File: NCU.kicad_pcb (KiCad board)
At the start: 2 copper layers, 22 parts, among them J2 USB_C_Receptacle_USB2.0_14P, J3 Micro_SD_Card, U1 STM32H745ZITx, U2 USB3300-EZK, U3 SN65HVD230, U4 SN65HVD230, U5 XL1509-3.3, U6 ESP32-C3-WROOM-02, U7 AP2112K-1.8, U8 LAN8742A

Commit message: work in progress
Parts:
- added C10: 100nF, Capacitor_SMD:C_0402_1005Metric_Pad0.74x0.62mm_HandSolder, F.Cu at (165.2, 59.0)
- added C11: 100nF, Capacitor_SMD:C_0402_1005Metric_Pad0.74x0.62mm_HandSolder, F.Cu at (165.2, 61.0)
- added C12: 100nF, Capacitor_SMD:C_0402_1005Metric_Pad0.74x0.62mm_HandSolder, F.Cu at (165.2, 62.9)
- added C13: 100nF, Capacitor_SMD:C_0402_1005Metric_Pad0.74x0.62mm_HandSolder, F.Cu at (165.2, 64.9)
- added C14: 100nF, Capacitor_SMD:C_0402_1005Metric_Pad0.74x0.62mm_HandSolder, F.Cu at (165.2, 66.9)
- added C15: 100nF, Capacitor_SMD:C_0402_1005Metric_Pad0.74x0.62mm_HandSolder, F.Cu at (165.2, 68.8)
- added C16: 100nF, Capacitor_SMD:C_0402_1005Metric_Pad0.74x0.62mm_HandSolder, F.Cu at (168.5, 57.0)
- added C17: 100nF, Capacitor_SMD:C_0402_1005Metric_Pad0.74x0.62mm_HandSolder, F.Cu at (168.5, 59.0)
- added C18: 100nF, Capacitor_SMD:C_0402_1005Metric_Pad0.74x0.62mm_HandSolder, F.Cu at (168.5, 61.0)
- added C19: 100nF, Capacitor_SMD:C_0402_1005Metric_Pad0.74x0.62mm_HandSolder, F.Cu at (168.5, 62.9)
- added C20: 100nF, Capacitor_SMD:C_0402_1005Metric_Pad0.74x0.62mm_HandSolder, F.Cu at (168.5, 64.9)
- added C21: 100nF, Capacitor_SMD:C_0402_1005Metric_Pad0.74x0.62mm_HandSolder, F.Cu at (168.5, 66.9)
- added C22: 100nF, Capacitor_SMD:C_0402_1005Metric_Pad0.74x0.62mm_HandSolder, F.Cu at (168.5, 68.8)
- added C23: 100nF, Capacitor_SMD:C_0402_1005Metric_Pad0.74x0.62mm_HandSolder, F.Cu at (171.7, 57.0)
- added C24: 100nF, Capacitor_SMD:C_0402_1005Metric_Pad0.74x0.62mm_HandSolder, F.Cu at (171.7, 59.0)
- added C25: 100nF, Capacitor_SMD:C_0402_1005Metric_Pad0.74x0.62mm_HandSolder, F.Cu at (171.7, 61.0)
- added C26: 100nF, Capacitor_SMD:C_0402_1005Metric_Pad0.74x0.62mm_HandSolder, F.Cu at (171.7, 62.9)
- added C27: 4.7uF, Capacitor_SMD:C_0402_1005Metric_Pad0.74x0.62mm_HandSolder, F.Cu at (171.7, 64.9)
- added C28: 200nF, Capacitor_SMD:C_0402_1005Metric_Pad0.74x0.62mm_HandSolder, F.Cu at (176.9, 57.0)
- added C29: 200nF, Capacitor_SMD:C_0402_1005Metric_Pad0.74x0.62mm_HandSolder, F.Cu at (176.9, 59.0)
- added C9: 4.7uF, Capacitor_SMD:C_0402_1005Metric_Pad0.74x0.62mm_HandSolder, F.Cu at (165.2, 57.0)
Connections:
- U1 pad 103: unconnected-(U1-VCAP-Pad103) -> Net-(C28-Pad1)
- U1 pad 104: Net-(U1-VSS-Pad104) -> GND
- U1 pad 105: unconnected-(U1-VDDLDO-Pad105) -> /MCU/3V3
- U1 pad 106: unconnected-(U1-VDD-Pad106) -> /MCU/3V3
- U1 pad 118: Net-(U1-VSS-Pad104) -> GND
- U1 pad 119: unconnected-(U1-VDD-Pad119) -> /MCU/3V3
- U1 pad 12: Net-(U1-VSS-Pad104) -> GND
- U1 pad 128: Net-(U1-VSS-Pad104) -> GND
- U1 pad 129: unconnected-(U1-VDD-Pad129) -> /MCU/3V3
- U1 pad 13: unconnected-(U1-VDD-Pad13) -> /MCU/3V3
- U1 pad 14: unconnected-(U1-VSSSMPS-Pad14) -> GND
- U1 pad 140: unconnected-(U1-VCAP-Pad140) -> Net-(C28-Pad1)
- U1 pad 141: Net-(U1-VSS-Pad104) -> GND
- U1 pad 143: unconnected-(U1-VDDLDO-Pad143) -> /MCU/3V3
- U1 pad 144: unconnected-(U1-VDD-Pad144) -> /MCU/3V3
- U1 pad 16: unconnected-(U1-VDDSMPS-Pad16) -> /MCU/MCU Power/VSSSMPS
- U1 pad 18: Net-(U1-VSS-Pad104) -> GND
- U1 pad 19: unconnected-(U1-VDD-Pad19) -> /MCU/3V3
- U1 pad 32: unconnected-(U1-VDD-Pad32) -> /MCU/3V3
- U1 pad 33: Net-(U1-VSS-Pad104) -> GND
- U1 pad 34: unconnected-(U1-VSSA-Pad34) -> GND
- U1 pad 36: unconnected-(U1-VDDA-Pad36) -> /MCU/3V3
- U1 pad 41: Net-(U1-VSS-Pad104) -> GND
- U1 pad 42: unconnected-(U1-VDD-Pad42) -> /MCU/3V3
- U1 pad 55: Net-(U1-VSS-Pad104) -> GND
- U1 pad 56: unconnected-(U1-VDD-Pad56) -> /MCU/3V3
- U1 pad 6: Net-(U1-VSS-Pad104) -> GND
- U1 pad 68: unconnected-(U1-VCAP-Pad68) -> Net-(C28-Pad1)
- U1 pad 69: Net-(U1-VSS-Pad104) -> GND
- U1 pad 7: unconnected-(U1-VDD-Pad7) -> /MCU/3V3
- U1 pad 70: unconnected-(U1-VDDLDO-Pad70) -> /MCU/3V3
- U1 pad 71: unconnected-(U1-VDD-Pad71) -> /MCU/3V3
- U1 pad 79: unconnected-(U1-VDD-Pad79) -> /MCU/3V3
- U1 pad 8: unconnected-(U1-VBAT-Pad8) -> /MCU/3V3
- U1 pad 80: Net-(U1-VSS-Pad104) -> GND
- U1 pad 89: Net-(U1-VSS-Pad104) -> GND
- U1 pad 90: unconnected-(U1-VDD50_USB-Pad90) -> /MCU/3V3
- U1 pad 91: unconnected-(U1-VDD33_USB-Pad91) -> /MCU/3V3
- U1 pad 92: unconnected-(U1-VDD-Pad92) -> /MCU/3V3

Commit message: wip
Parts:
- added C30: 100nF, Capacitor_SMD:C_0402_1005Metric_Pad0.74x0.62mm_HandSolder, F.Cu at (96.2, 65.1)
- added J1: RJ45, Connector_RJ:RJ45_Hanrun_HR911105A_Horizontal, F.Cu at (75.3, 43.8)
- added J3: Micro_SD_Card, Connector_Card:microSD_HC_Molex_47219-2001, F.Cu at (98.1, 46.8)
- added U9: BG95-M3, RF_GSM:Quectel_BG95, F.Cu at (81.2, 77.4)
- C23, C25: value 100nF -> 1uF
- C28, C29: value 200nF -> 2.2uF
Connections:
- net Net-(J2-CC1) renamed /USB/CC1
- net Net-(J2-CC2) renamed /USB/CC2
- net Net-(J2-D+-PadA6) renamed /USB/D+
- net Net-(J2-D--PadA7) renamed /USB/D-
- C27 pad 2: /MCU/MCU Power/VSSSMPS -> GND
- U1 pad 16: /MCU/MCU Power/VSSSMPS -> /MCU/3V3

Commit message: updated to use RMII and routed ethernet and CAN from micro
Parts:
- added C31: 220pF, Capacitor_SMD:C_0402_1005Metric_Pad0.74x0.62mm_HandSolder, F.Cu at (117.1, 49.0)
- added C32: 10uF, Capacitor_SMD:C_0402_1005Metric_Pad0.74x0.62mm_HandSolder, F.Cu at (117.1, 51.0)
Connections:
- C10 pad 1: /MCU/3V3 -> +3V3
- C11 pad 1: /MCU/3V3 -> +3V3
- C12 pad 1: /MCU/3V3 -> +3V3
- C13 pad 1: /MCU/3V3 -> +3V3
- C14 pad 1: /MCU/3V3 -> +3V3
- C15 pad 1: /MCU/3V3 -> +3V3
- C16 pad 1: /MCU/3V3 -> +3V3
- C17 pad 1: /MCU/3V3 -> +3V3
- C18 pad 1: /MCU/3V3 -> +3V3
- C19 pad 1: /MCU/3V3 -> +3V3
- C20 pad 1: /MCU/3V3 -> +3V3
- C21 pad 1: /MCU/3V3 -> +3V3
- C22 pad 1: /MCU/3V3 -> +3V3
- C23 pad 1: /MCU/3V3 -> +3V3
- C24 pad 1: /MCU/3V3 -> +3V3
- C25 pad 1: /MCU/3V3 -> +3V3
- C26 pad 1: /MCU/3V3 -> +3V3
- C27 pad 1: /MCU/3V3 -> +3V3
- C30 pad 1: /MCU/3V3 -> +3V3
- C9 pad 1: /MCU/3V3 -> +3V3
- U1 pad 105: /MCU/3V3 -> +3V3
- U1 pad 106: /MCU/3V3 -> +3V3
- U1 pad 112: unconnected-(U1-PD0-Pad112) -> /MCU/FDCAN1_RX
- U1 pad 113: unconnected-(U1-PD1-Pad113) -> /MCU/FDCAN1_TX
- U1 pad 119: /MCU/3V3 -> +3V3
- U1 pad 129: /MCU/3V3 -> +3V3
- U1 pad 13: /MCU/3V3 -> +3V3
- U1 pad 132: unconnected-(U1-PB5-Pad132) -> /MCU/FDCAN2_RX
- U1 pad 133: unconnected-(U1-PB6-Pad133) -> /MCU/FDCAN2_TX
- U1 pad 143: /MCU/3V3 -> +3V3
- U1 pad 144: /MCU/3V3 -> +3V3
- U1 pad 15: unconnected-(U1-VLXSMPS-Pad15) -> Net-(U1-VLXSMPS)
- U1 pad 16: /MCU/3V3 -> +3V3
- U1 pad 17: unconnected-(U1-VFBSMPS-Pad17) -> Net-(U1-VFBSMPS)
- U1 pad 19: /MCU/3V3 -> +3V3
- U1 pad 29: unconnected-(U1-PC1-Pad29) -> /MCU/ETH_MDC
- U1 pad 32: /MCU/3V3 -> +3V3
- U1 pad 35: unconnected-(U1-VREF+-Pad35) -> +3V3
- U1 pad 36: /MCU/3V3 -> +3V3
- U1 pad 39: unconnected-(U1-PA2-Pad39) -> /MCU/ETH_MDIO
- U1 pad 42: /MCU/3V3 -> +3V3
- U1 pad 46: unconnected-(U1-PA7-Pad46) -> /MCU/ETH_CRS_DV
- U1 pad 47: unconnected-(U1-PC4-Pad47) -> /MCU/ETH_RXD0
- U1 pad 48: unconnected-(U1-PC5-Pad48) -> /MCU/ETH_RXD1
- U1 pad 56: /MCU/3V3 -> +3V3
- U1 pad 67: unconnected-(U1-PB11-Pad67) -> /MCU/ETH_TX_EN
- U1 pad 7: /MCU/3V3 -> +3V3
- U1 pad 70: /MCU/3V3 -> +3V3
- U1 pad 71: /MCU/3V3 -> +3V3
- U1 pad 72: unconnected-(U1-PB12-Pad72) -> /MCU/ETH_TXD0
- U1 pad 73: unconnected-(U1-PB13-Pad73) -> /MCU/ETH_TXD1
- U1 pad 79: /MCU/3V3 -> +3V3
- U1 pad 8: /MCU/3V3 -> +3V3
- U1 pad 90: /MCU/3V3 -> +3V3
- U1 pad 91: /MCU/3V3 -> +3V3
- U1 pad 92: /MCU/3V3 -> +3V3
- U8 pad 10: unconnected-(U8-RXER/PHYAD0-Pad10) -> GND
- U8 pad 11: unconnected-(U8-CRS_DV/MODE2-Pad11) -> /MCU/ETH_CRS_DV
- U8 pad 12: unconnected-(U8-MDIO-Pad12) -> /MCU/ETH_MDIO
- U8 pad 13: unconnected-(U8-MDC-Pad13) -> /MCU/ETH_MDC
- U8 pad 16: unconnected-(U8-TXEN-Pad16) -> /MCU/ETH_TX_EN
- U8 pad 17: unconnected-(U8-TXD0-Pad17) -> /MCU/ETH_TXD0
- U8 pad 18: unconnected-(U8-TXD1-Pad18) -> /MCU/ETH_TXD1
- U8 pad 7: unconnected-(U8-RXD1/MODE1-Pad7) -> /MCU/ETH_RXD1
- U8 pad 8: unconnected-(U8-RXD0/MODE0-Pad8) -> /MCU/ETH_RXD0

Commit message: full initial power scheme
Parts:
- added C33: 4.7uF, Capacitor_SMD:C_1210_3225Metric_Pad1.33x2.70mm_HandSolder, F.Cu at (110.1, 113.8)
- added C34: 4.7uF, Capacitor_SMD:C_1210_3225Metric_Pad1.33x2.70mm_HandSolder, F.Cu at (110.1, 118.0)
- added C35: 0.1uF, Capacitor_SMD:C_0603_1608Metric_Pad1.08x0.95mm_HandSolder, F.Cu at (118.5, 122.4)
- added C36: 0.1uF, Capacitor_SMD:C_0402_1005Metric_Pad0.74x0.62mm_HandSolder, F.Cu at (118.0, 124.7)
- added C37: 33pF, Capacitor_SMD:C_0402_1005Metric_Pad0.74x0.62mm_HandSolder, F.Cu at (118.0, 126.6)
- added C38: 47uF, Capacitor_SMD:C_1210_3225Metric_Pad1.33x2.70mm_HandSolder, F.Cu at (110.1, 122.2)
- added C39: 47uF, Capacitor_SMD:C_1210_3225Metric_Pad1.33x2.70mm_HandSolder, F.Cu at (110.1, 126.5)
- added IC1: LMR51460SQDRRRQ1, SamacSys_Parts:SON50P300X300X80-13N-D, F.Cu at (126.5, 127.5)
- added IC2: TPS628101HQWRWYRQ1, SamacSys_Parts:TPS6281008QWRWYRQ1, F.Cu at (99.0, 120.1)
- added L1: 0.47uH, SamacSys_Parts:INDPM7066X240N, F.Cu at (134.5, 119.5)
- added L3: 4.7uH, Inductor_SMD:L_Coilcraft_XAL7030-472, F.Cu at (121.1, 116.4)
- added Q1: CSD25483F4, SamacSys_Parts:CSD25483F4T, F.Cu at (136.2, 129.3)
- added Q2: CSD25483F4, SamacSys_Parts:CSD25483F4T, F.Cu at (136.2, 133.0)
- added R1: 100k, Resistor_SMD:R_0402_1005Metric_Pad0.72x0.64mm_HandSolder, F.Cu at (114.7, 112.6)
- added R2: 19.1k, Resistor_SMD:R_0402_1005Metric_Pad0.72x0.64mm_HandSolder, F.Cu at (114.7, 114.6)
- added R3: 1k, Resistor_SMD:R_0402_1005Metric_Pad0.72x0.64mm_HandSolder, F.Cu at (114.7, 116.6)
- added R4: 100k, Resistor_SMD:R_0402_1005Metric_Pad0.72x0.64mm_HandSolder, F.Cu at (114.7, 118.6)
- added R5: 10k, Resistor_SMD:R_0402_1005Metric_Pad0.72x0.64mm_HandSolder, F.Cu at (114.7, 120.6)
- added R6: 100k, Resistor_SMD:R_0402_1005Metric_Pad0.72x0.64mm_HandSolder, F.Cu at (114.7, 122.6)
- added R7: 10k, Resistor_SMD:R_0402_1005Metric_Pad0.72x0.64mm_HandSolder, F.Cu at (114.7, 124.6)
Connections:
- U1 pad 100: unconnected-(U1-PA11-Pad100) -> /MCU/USB_OTG_FS_DM
- U1 pad 101: unconnected-(U1-PA12-Pad101) -> /MCU/USB_OTG_FS_DP
- U1 pad 98: unconnected-(U1-PA9-Pad98) -> /MCU/USB_OTG_FS_VBUS
- U3 pad 1: /CAN/CAN0_TX -> /MCU/FDCAN1_TX
- U3 pad 4: /CAN/CAN0_RX -> /MCU/FDCAN1_RX
- U4 pad 1: /CAN/CAN1_TX -> /MCU/FDCAN2_TX
- U4 pad 4: /CAN/CAN1_RX -> /MCU/FDCAN2_RX

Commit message: added lib to project and added molex superseal connector
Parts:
- added C40: 4.7nF, Capacitor_SMD:C_0402_1005Metric_Pad0.74x0.62mm_HandSolder, F.Cu at (88.7, 132.2)
- added C41: 10pF, Capacitor_SMD:C_0402_1005Metric_Pad0.74x0.62mm_HandSolder, F.Cu at (88.7, 134.2)
- added C42: 100nF, Capacitor_SMD:C_0402_1005Metric_Pad0.74x0.62mm_HandSolder, F.Cu at (85.7, 97.6)
- added C43: 100nF, Capacitor_SMD:C_0402_1005Metric_Pad0.74x0.62mm_HandSolder, F.Cu at (85.7, 99.6)
- added C44: 100nF, Capacitor_SMD:C_0402_1005Metric_Pad0.74x0.62mm_HandSolder, F.Cu at (85.7, 101.5)
- added C45: 100nF, Capacitor_SMD:C_0402_1005Metric_Pad0.74x0.62mm_HandSolder, F.Cu at (85.7, 103.5)
- added C46: 100nF, Capacitor_SMD:C_0402_1005Metric_Pad0.74x0.62mm_HandSolder, F.Cu at (85.7, 105.5)
- added C47: 100nF, Capacitor_SMD:C_0402_1005Metric_Pad0.74x0.62mm_HandSolder, F.Cu at (85.7, 107.5)
- added C48: 100nF, Capacitor_SMD:C_0402_1005Metric_Pad0.74x0.62mm_HandSolder, F.Cu at (85.7, 109.4)
- added C49: 100nF, Capacitor_SMD:C_0402_1005Metric_Pad0.74x0.62mm_HandSolder, F.Cu at (85.7, 111.4)
- added C5: 22uF, Inductor_SMD:L_1206_3216Metric_Pad1.22x1.90mm_HandSolder, F.Cu at (80.8, 130.4)
- added C50: 100nF, Capacitor_SMD:C_0402_1005Metric_Pad0.74x0.62mm_HandSolder, F.Cu at (85.7, 113.4)
- added C6: 22uF, Inductor_SMD:L_1206_3216Metric_Pad1.22x1.90mm_HandSolder, F.Cu at (80.8, 133.9)
- added C7: 22uF, Inductor_SMD:L_1206_3216Metric_Pad1.22x1.90mm_HandSolder, F.Cu at (80.8, 137.3)
- added C8: 22uF, Capacitor_SMD:C_0603_1608Metric_Pad1.08x0.95mm_HandSolder, F.Cu at (86.0, 129.9)
- added D1: BZV55C3V6, Diode_SMD:D_MiniMELF, F.Cu at (81.0, 98.3)
- added D2: BZV55C3V6, Diode_SMD:D_MiniMELF, F.Cu at (81.0, 101.6)
- added D3: BZV55C3V6, Diode_SMD:D_MiniMELF, F.Cu at (81.0, 105.0)
- added D4: BZV55C3V6, Diode_SMD:D_MiniMELF, F.Cu at (81.0, 108.3)
- added D5: BZV55C3V6, Diode_SMD:D_MiniMELF, F.Cu at (81.0, 111.7)
- added D6: BZV55C3V6, Diode_SMD:D_MiniMELF, F.Cu at (81.0, 115.0)
- added D7: BZV55C3V6, Diode_SMD:D_MiniMELF, F.Cu at (81.0, 118.3)
- added D8: BZV55C3V6, Diode_SMD:D_MiniMELF, F.Cu at (81.0, 121.7)
- added D9: BZV55C3V6, Diode_SMD:D_MiniMELF, F.Cu at (81.0, 125.0)
- added J2: USB_B, Connector_USB:USB_B_Lumberg_2411_02_Horizontal, F.Cu at (31.6, 142.2)
- added J4: 6437288-1, SamacSys_Parts:6437288-1, F.Cu at (52.4, 97.4)
- added NT1: NetTie_2, NetTie:NetTie-2_SMD_Pad0.5mm, F.Cu at (88.4, 135.9)
- added R10: 19.6k, Resistor_SMD:R_0402_1005Metric_Pad0.72x0.64mm_HandSolder, F.Cu at (85.5, 136.2)
- added R11: 100k, Resistor_SMD:R_0402_1005Metric_Pad0.72x0.64mm_HandSolder, F.Cu at (85.5, 138.2)
- added R12: 100k, Resistor_SMD:R_0402_1005Metric_Pad0.72x0.64mm_HandSolder, F.Cu at (85.5, 140.2)
- added R13: 100, Capacitor_SMD:C_0402_1005Metric_Pad0.74x0.62mm_HandSolder, F.Cu at (89.0, 97.6)
- added R14: 10k, Capacitor_SMD:C_0402_1005Metric_Pad0.74x0.62mm_HandSolder, F.Cu at (89.0, 99.6)
- added R15: 20k, Capacitor_SMD:C_0402_1005Metric_Pad0.74x0.62mm_HandSolder, F.Cu at (89.0, 101.5)
- added R16: 10k, Capacitor_SMD:C_0402_1005Metric_Pad0.74x0.62mm_HandSolder, F.Cu at (89.0, 103.5)
- added R17: 20k, Capacitor_SMD:C_0402_1005Metric_Pad0.74x0.62mm_HandSolder, F.Cu at (89.0, 105.5)
- added R18: 100, Capacitor_SMD:C_0402_1005Metric_Pad0.74x0.62mm_HandSolder, F.Cu at (89.0, 107.5)
- added R19: 10k, Capacitor_SMD:C_0402_1005Metric_Pad0.74x0.62mm_HandSolder, F.Cu at (89.0, 109.4)
- added R20: 20k, Capacitor_SMD:C_0402_1005Metric_Pad0.74x0.62mm_HandSolder, F.Cu at (89.0, 111.4)
- added R21: 100, Capacitor_SMD:C_0402_1005Metric_Pad0.74x0.62mm_HandSolder, F.Cu at (89.0, 113.4)
- added R22: 10k, Capacitor_SMD:C_0402_1005Metric_Pad0.74x0.62mm_HandSolder, F.Cu at (92.2, 97.6)
- added R23: 20k, Capacitor_SMD:C_0402_1005Metric_Pad0.74x0.62mm_HandSolder, F.Cu at (92.2, 99.6)
- added R24: 100, Capacitor_SMD:C_0402_1005Metric_Pad0.74x0.62mm_HandSolder, F.Cu at (92.2, 101.5)
- added R25: 10k, Capacitor_SMD:C_0402_1005Metric_Pad0.74x0.62mm_HandSolder, F.Cu at (92.2, 103.5)
- added R26: 20k, Capacitor_SMD:C_0402_1005Metric_Pad0.74x0.62mm_HandSolder, F.Cu at (92.2, 105.5)
- added R27: 100, Capacitor_SMD:C_0402_1005Metric_Pad0.74x0.62mm_HandSolder, F.Cu at (92.2, 107.5)
- added R28: 10k, Capacitor_SMD:C_0402_1005Metric_Pad0.74x0.62mm_HandSolder, F.Cu at (92.2, 109.4)
- added R29: 20k, Capacitor_SMD:C_0402_1005Metric_Pad0.74x0.62mm_HandSolder, F.Cu at (92.2, 111.4)
- added R30: 100, Capacitor_SMD:C_0402_1005Metric_Pad0.74x0.62mm_HandSolder, F.Cu at (92.2, 113.4)
- added R31: 10k, Capacitor_SMD:C_0402_1005Metric_Pad0.74x0.62mm_HandSolder, F.Cu at (95.4, 97.6)
- added R32: 20k, Capacitor_SMD:C_0402_1005Metric_Pad0.74x0.62mm_HandSolder, F.Cu at (95.4, 99.6)
- added R33: 100, Capacitor_SMD:C_0402_1005Metric_Pad0.74x0.62mm_HandSolder, F.Cu at (95.4, 101.5)
- added R34: 10k, Capacitor_SMD:C_0402_1005Metric_Pad0.74x0.62mm_HandSolder, F.Cu at (95.4, 103.5)
- added R35: 20k, Capacitor_SMD:C_0402_1005Metric_Pad0.74x0.62mm_HandSolder, F.Cu at (95.4, 105.5)
- added R36: 100, Capacitor_SMD:C_0402_1005Metric_Pad0.74x0.62mm_HandSolder, F.Cu at (95.4, 107.5)
- added R37: 10k, Capacitor_SMD:C_0402_1005Metric_Pad0.74x0.62mm_HandSolder, F.Cu at (95.4, 109.4)
- added R38: 20k, Capacitor_SMD:C_0402_1005Metric_Pad0.74x0.62mm_HandSolder, F.Cu at (95.4, 111.4)
- added R39: 100, Capacitor_SMD:C_0402_1005Metric_Pad0.74x0.62mm_HandSolder, F.Cu at (95.4, 113.4)
- added R8: 8.06k, Resistor_SMD:R_0402_1005Metric_Pad0.72x0.64mm_HandSolder, F.Cu at (85.5, 132.2)
- added R9: 88.7k, Resistor_SMD:R_0402_1005Metric_Pad0.72x0.64mm_HandSolder, F.Cu at (85.5, 134.2)
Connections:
- net /Power Supplies/SW_FB renamed /Power Supplies/LMR_FB
- IC1 pad 5: unconnected-(IC1-PG-Pad5) -> /Power Supplies/12V_PG
- IC2 pad 1: unconnected-(IC2-MODE/SYNC_1-Pad1) -> +5V
- IC2 pad 10: unconnected-(IC2-MODE/SYNC_2-Pad10) -> +5V
- IC2 pad 11: unconnected-(IC2-FB_2-Pad11) -> /Power Supplies/TPS_FB
- IC2 pad 12: unconnected-(IC2-COMP/_FSET_2-Pad12) -> /Power Supplies/TPS_CF
- IC2 pad 13: unconnected-(IC2-EN_2-Pad13) -> +5V
- IC2 pad 2: unconnected-(IC2-VIN-Pad2) -> +5V
- IC2 pad 3: unconnected-(IC2-SW-Pad3) -> Net-(IC2-SW)
- IC2 pad 4: unconnected-(IC2-GND-Pad4) -> GND
- IC2 pad 5: unconnected-(IC2-FB_1-Pad5) -> /Power Supplies/TPS_FB
- IC2 pad 6: unconnected-(IC2-SS/TR-Pad6) -> Net-(IC2-SS/TR)
- IC2 pad 7: unconnected-(IC2-COMP/_FSET_1-Pad7) -> /Power Supplies/TPS_CF
- IC2 pad 8: unconnected-(IC2-EN_1-Pad8) -> +5V
- IC2 pad 9: unconnected-(IC2-PG-Pad9) -> /Power Supplies/3V3_PG
- L1 pad 1: unconnected-(L1-Pad1) -> Net-(IC2-SW)
- L1 pad 2: unconnected-(L1-Pad2) -> +3V3

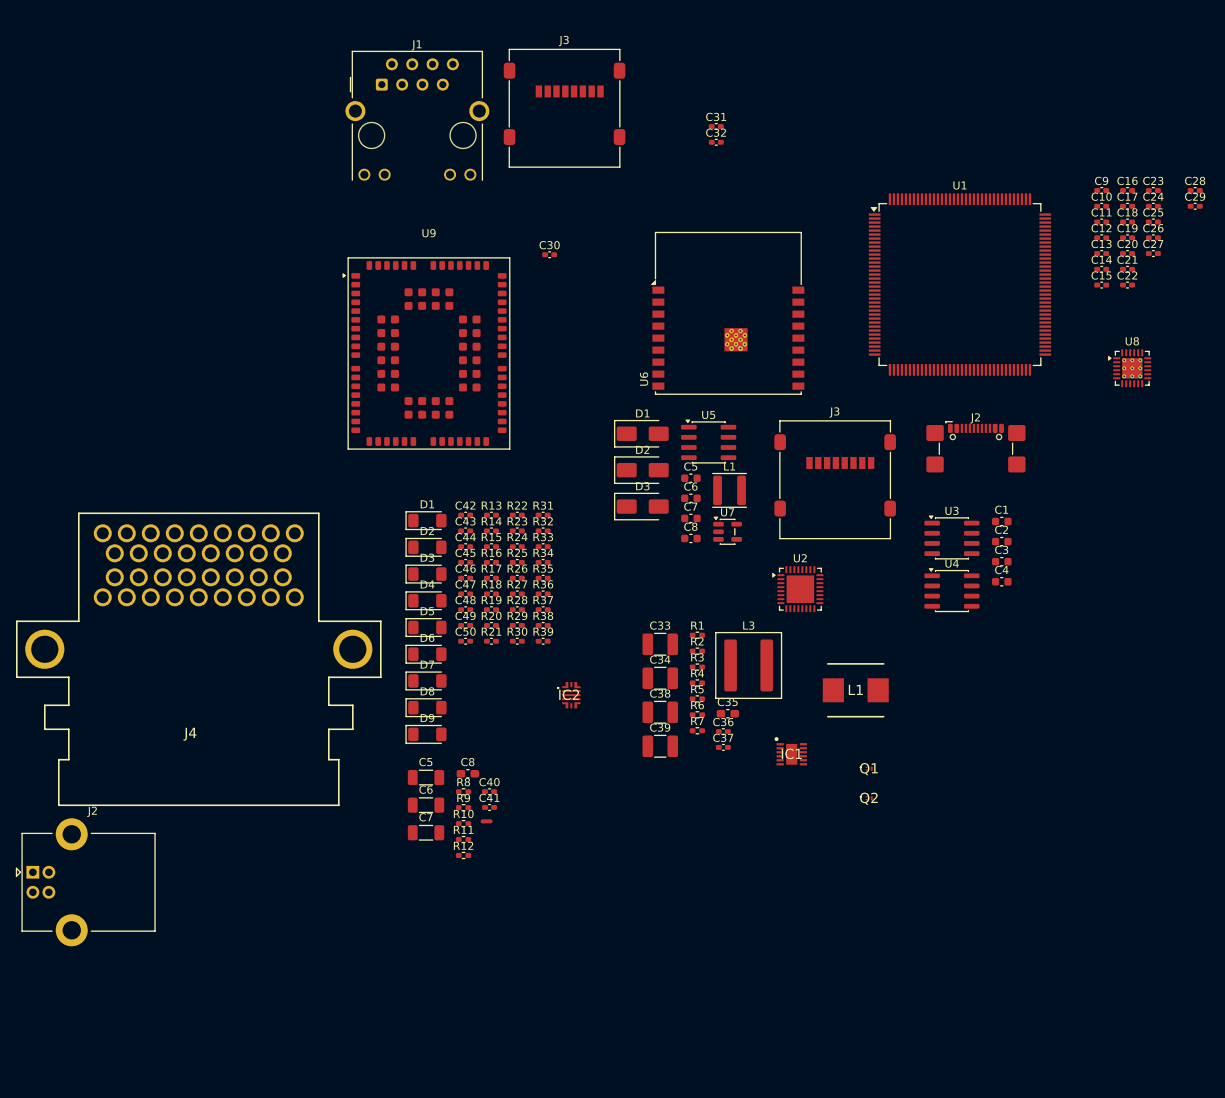
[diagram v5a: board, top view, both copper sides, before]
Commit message: added connects schematic, which is looking quite good
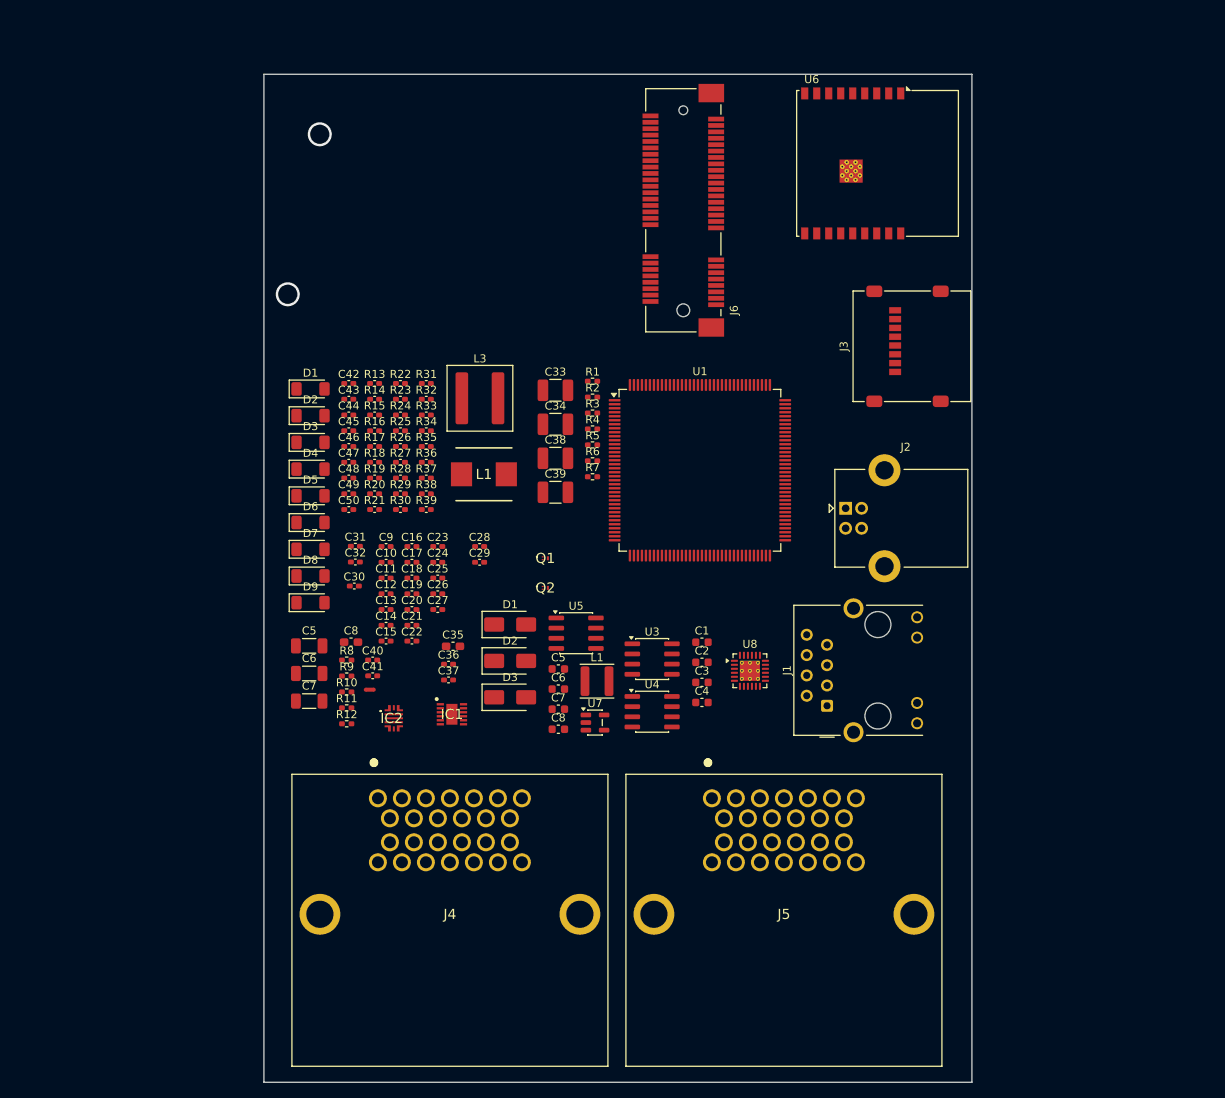
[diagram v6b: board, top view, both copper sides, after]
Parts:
- removed the J2 at (149.5, 90.4)
- removed the J3 at (98.1, 46.8)
- removed U2: USB3300-EZK, Package_DFN_QFN:QFN-32-1EP_5x5mm_P0.5mm_EP3.45x3.45mm
- removed U9: BG95-M3, RF_GSM:Quectel_BG95
- added J5: 6437288-4, SamacSys_Parts:64372884, F.Cu at (116.5, 133.0)
- added J6: Bus_PCI_Express_Mini, Connector_PCBEdge:BUS_PCI_Express_Mini_Full, F.Cu at (112.9, 59.5)
- J4: value 6437288-1 -> 6437288-4; footprint SamacSys_Parts:6437288-1 -> SamacSys_Parts:64372884
- moved J2 111.3 mm to (133.2, 96.8)
- moved C10 99.9 mm to (75.8, 103.5)
- moved C11 99.9 mm to (75.8, 105.5)
- moved C12 99.9 mm to (75.8, 107.4)
- moved C13 99.9 mm to (75.8, 109.4)
- moved C14 99.9 mm to (75.8, 111.4)
- moved C15 99.9 mm to (75.8, 113.3)
- moved C16 99.9 mm to (79.0, 101.5)
- moved C17 99.9 mm to (79.0, 103.5)
- moved C18 99.9 mm to (79.0, 105.5)
- moved C19 99.9 mm to (79.0, 107.4)
- moved C20 99.9 mm to (79.0, 109.4)
- moved C21 99.9 mm to (79.0, 111.4)
- moved C22 99.9 mm to (79.0, 113.3)
- moved C28 99.9 mm to (87.5, 101.5)
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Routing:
- net (no net): vias 0 -> 2
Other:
- board outline added: 88.5 x 126 mm
